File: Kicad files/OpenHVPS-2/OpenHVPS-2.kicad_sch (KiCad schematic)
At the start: 69 parts, among them J1 Conn_01x03_Male, J2 Conn_01x03_Male, Q1 FQT7N10, Q2 BC846A, Q3 MMDT3906, U1 MAX6008AEUR+T, U2 74HC14, U3 MAX4162, U4 CD14538BM

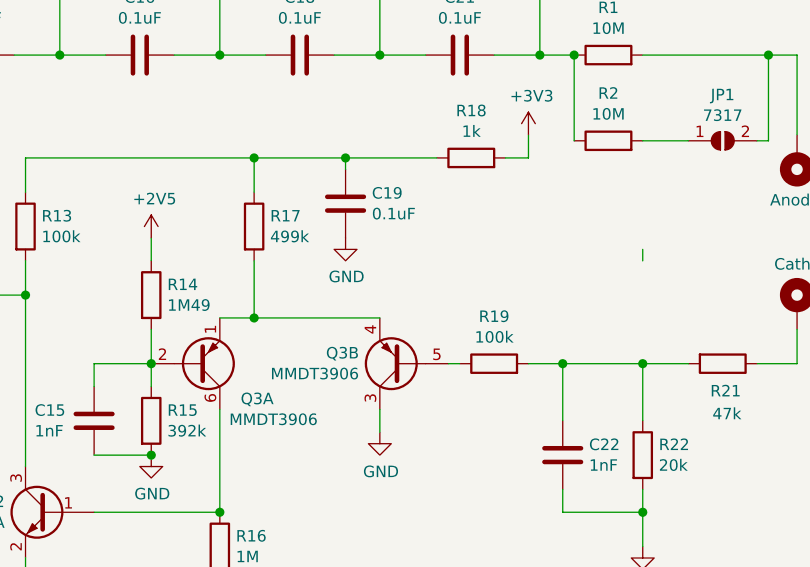
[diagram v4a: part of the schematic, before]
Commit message: Created BOM. updated component markings
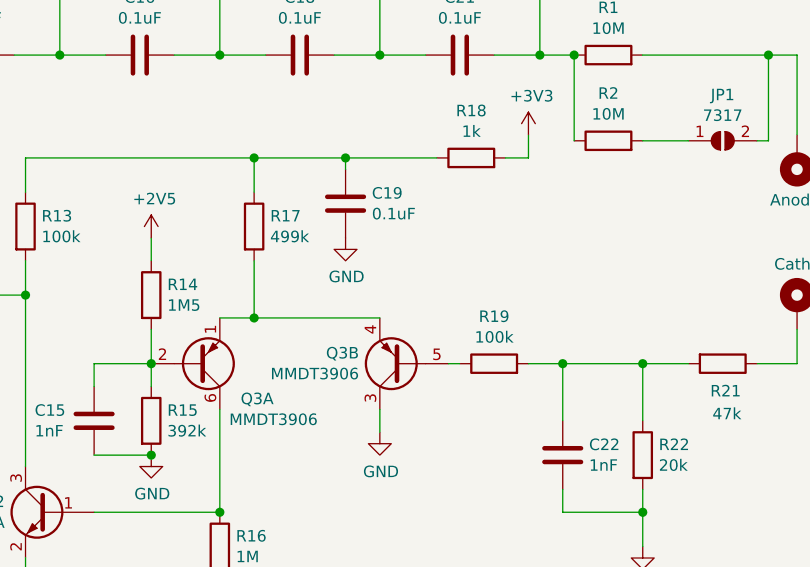
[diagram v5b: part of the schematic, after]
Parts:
- R14: value 1M49 -> 1M5
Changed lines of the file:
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@@
   (title_block
     (title "SafePulse")
-    (date "2021-01-15")
-    (rev "2.0")
+    (date "2021-01-17")
+    (rev "2.01")
     (company "SafeCast")
     (comment 1 "Double Sided Version")
@@
     (stroke (width 0) (type solid) (color 0 0 0 0))
   )
-  (wire (pts (xy 261.62 122.555) (xy 261.62 121.285))
-    (stroke (width 0) (type solid) (color 0 0 0 0))
-  )
   (wire (pts (xy 261.62 133.985) (xy 261.62 140.335))
     (stroke (width 0) (type solid) (color 0 0 0 0))
@@
       (effects (font (size 1.27 1.27)) hide)
     )
-    (property "Datasheet" "~" (id 3) (at 30.48 178.435 0)
+    (property "Datasheet" "https://www.digikey.com/en/products/detail/yageo/RC0805FR-073M16L/727809" (id 3) (at 30.48 178.435 0)
       (effects (font (size 1.27 1.27)) hide)
     )
@@
       (effects (font (size 1.27 1.27)) hide)
     )
-    (property "Datasheet" "~" (id 3) (at 40.64 125.095 0)
+    (property "Datasheet" "https://www.digikey.com/en/products/detail/yageo/RT0805FRE07560KL/1079317" (id 3) (at 40.64 125.095 0)
       (effects (font (size 1.27 1.27)) hide)
     )
@@
       (effects (font (size 1.27 1.27)) hide)
     )
-    (property "Datasheet" "~" (id 3) (at 53.34 99.695 0)
+    (property "Datasheet" "https://www.digikey.com/en/products/detail/stackpole-electronics-inc/RMCF0805FT100K/1760712" (id 3) (at 53.34 99.695 0)
       (effects (font (size 1.27 1.27)) hide)
     )
@@
       (effects (font (size 1.27 1.27)) hide)
     )
-    (property "Datasheet" "~" (id 3) (at 60.96 74.295 0)
+    (property "Datasheet" "https://www.digikey.com/en/products/detail/stackpole-electronics-inc/RMCF0805FT100K/1760712" (id 3) (at 60.96 74.295 0)
       (effects (font (size 1.27 1.27)) hide)
     )
@@
       (effects (font (size 1.27 1.27)) hide)
     )
-    (property "Datasheet" "~" (id 3) (at 71.12 37.465 0)
+    (property "Datasheet" "https://www.digikey.com/en/products/detail/te-connectivity-passive-product/CRG0805F100R/2380830" (id 3) (at 71.12 37.465 0)
       (effects (font (size 1.27 1.27)) hide)
     )
@@
       (effects (font (size 1.27 1.27)) hide)
     )
-    (property "Datasheet" "~" (id 3) (at 101.6 146.685 0)
+    (property "Datasheet" "https://www.digikey.com/en/products/detail/koa-speer-electronics-inc/RK73H2ATTD1213F/10235721" (id 3) (at 101.6 146.685 0)
       (effects (font (size 1.27 1.27)) hide)
     )
@@
       (effects (font (size 1.27 1.27)) hide)
     )
-    (property "Datasheet" "~" (id 3) (at 116.84 121.285 0)
+    (property "Datasheet" "https://www.digikey.com/en/products/detail/stackpole-electronics-inc/RMCF0805FT22M0/6053747" (id 3) (at 116.84 121.285 0)
       (effects (font (size 1.27 1.27)) hide)
     )
@@
       (effects (font (size 1.27 1.27)) hide)
     )
-    (property "Datasheet" "~" (id 3) (at 127 121.285 0)
+    (property "Datasheet" "https://www.digikey.com/en/products/detail/stackpole-electronics-inc/RMCF0805FT22M0/6053747" (id 3) (at 127 121.285 0)
       (effects (font (size 1.27 1.27)) hide)
     )
@@
       (effects (font (size 1.27 1.27)) hide)
     )
-    (property "Datasheet" "~" (id 3) (at 137.16 121.285 0)
+    (property "Datasheet" "https://www.digikey.com/en/products/detail/stackpole-electronics-inc/RMCF0805FT22M0/6053747" (id 3) (at 137.16 121.285 0)
       (effects (font (size 1.27 1.27)) hide)
     )
@@
       (effects (font (size 1.27 1.27)) hide)
     )
-    (property "Datasheet" "~" (id 3) (at 143.51 109.855 0)
+    (property "Datasheet" "https://www.digikey.com/en/products/detail/stackpole-electronics-inc/RMCF0805FT22M0/6053747" (id 3) (at 143.51 109.855 0)
       (effects (font (size 1.27 1.27)) hide)
     )
@@
       (effects (font (size 1.27 1.27)) hide)
     )
-    (property "Datasheet" "~" (id 3) (at 161.29 126.365 0)
+    (property "Datasheet" "https://www.digikey.com/en/products/detail/te-connectivity-passive-product/CRGCQ0805F33K/8576369" (id 3) (at 161.29 126.365 0)
       (effects (font (size 1.27 1.27)) hide)
     )
@@
       (effects (font (size 1.27 1.27)) hide)
     )
-    (property "Datasheet" "~" (id 3) (at 177.8 137.795 0)
+    (property "Datasheet" "https://www.digikey.com/en/products/detail/te-connectivity-passive-product/CRG0805F100R/2380830" (id 3) (at 177.8 137.795 0)
       (effects (font (size 1.27 1.27)) hide)
     )
@@
       (effects (font (size 1.27 1.27)) hide)
     )
-    (property "Datasheet" "~" (id 3) (at 193.04 118.745 0)
+    (property "Datasheet" "https://www.digikey.com/en/products/detail/stackpole-electronics-inc/RMCF0805FT100K/1760712" (id 3) (at 193.04 118.745 0)
       (effects (font (size 1.27 1.27)) hide)
     )
@@
       (effects (font (size 1.27 1.27)) (justify left))
     )
-    (property "Value" "1M49" (id 1) (at 208.788 127.514 0)
+    (property "Value" "1M5" (id 1) (at 208.788 127.514 0)
       (effects (font (size 1.27 1.27)) (justify left))
     )
@@
       (effects (font (size 1.27 1.27)) hide)
     )
-    (property "Datasheet" "~" (id 3) (at 207.01 126.365 0)
+    (property "Datasheet" "https://www.digikey.com/en/products/detail/vishay-dale/CRCW08051M50FKEA/1176034" (id 3) (at 207.01 126.365 0)
       (effects (font (size 1.27 1.27)) hide)
     )
@@
       (effects (font (size 1.27 1.27)) hide)
     )
-    (property "Datasheet" "~" (id 3) (at 207.01 140.335 0)
+    (property "Datasheet" "https://www.digikey.com/en/products/detail/yageo/RC0805FR-07392KL/727905" (id 3) (at 207.01 140.335 0)
       (effects (font (size 1.27 1.27)) hide)
     )
@@
       (effects (font (size 1.27 1.27)) hide)
     )
-    (property "Datasheet" "~" (id 3) (at 214.63 154.305 0)
+    (property "Datasheet" "https://www.digikey.com/en/products/detail/yageo/RT0805FRE071ML/1079056" (id 3) (at 214.63 154.305 0)
       (effects (font (size 1.27 1.27)) hide)
     )
@@
       (effects (font (size 1.27 1.27)) hide)
     )
-    (property "Datasheet" "~" (id 3) (at 218.44 118.745 0)
+    (property "Datasheet" "https://www.digikey.com/en/products/detail/stackpole-electronics-inc/RMCF0805FT499K/1760301" (id 3) (at 218.44 118.745 0)
       (effects (font (size 1.27 1.27)) hide)
     )
@@
       (effects (font (size 1.27 1.27)) hide)
     )
-    (property "Datasheet" "~" (id 3) (at 242.57 111.125 0)
+    (property "Datasheet" "https://www.digikey.com/en/products/detail/yageo/RT0805FRE071KL/1079055" (id 3) (at 242.57 111.125 0)
       (effects (font (size 1.27 1.27)) hide)
     )
@@
       (effects (font (size 1.27 1.27)) hide)
     )
-    (property "Datasheet" "~" (id 3) (at 245.11 133.985 0)
+    (property "Datasheet" "https://www.digikey.com/en/products/detail/stackpole-electronics-inc/RMCF0805FT100K/1760712" (id 3) (at 245.11 133.985 0)
       (effects (font (size 1.27 1.27)) hide)
     )
@@
       (effects (font (size 1.27 1.27)) hide)
     )
-    (property "Datasheet" "~" (id 3) (at 261.62 144.145 0)
+    (property "Datasheet" "https://www.digikey.com/en/products/detail/panasonic-electronic-components/ERJ-6ENF2002V/111532" (id 3) (at 261.62 144.145 0)
       (effects (font (size 1.27 1.27)) hide)
     )
@@
       (effects (font (size 1.27 1.27)) hide)
     )
-    (property "Datasheet" "~" (id 3) (at 270.51 133.985 0)
+    (property "Datasheet" "https://www.digikey.com/en/products/detail/yageo/RC0805FR-0747KL/727973" (id 3) (at 270.51 133.985 0)
       (effects (font (size 1.27 1.27)) hide)
     )
@@
     )
     (path "/adcc374e-3c86-48f4-8335-00f8a4e67511"
-      (reference "R14") (unit 1) (value "1M49") (footprint "Resistor_SMD:R_0805_2012Metric")
+      (reference "R14") (unit 1) (value "1M5") (footprint "Resistor_SMD:R_0805_2012Metric")
     )
     (path "/69a31fa7-1f19-4a47-87b1-54ebf66883f6"

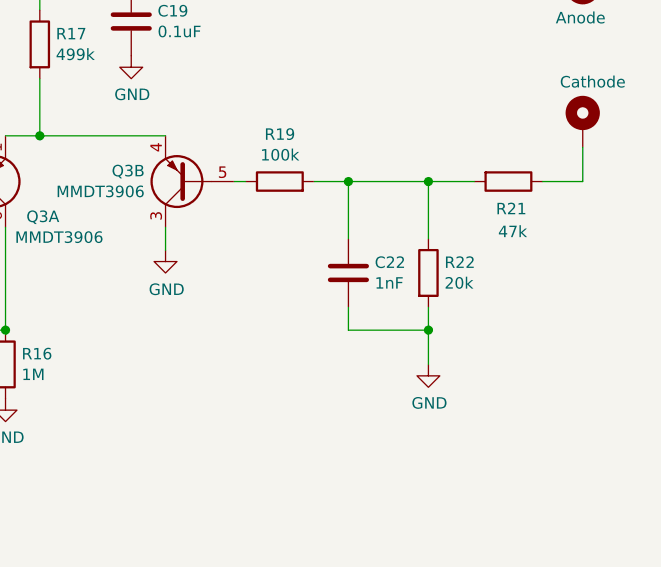
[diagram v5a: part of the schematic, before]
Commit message: updated C22 value
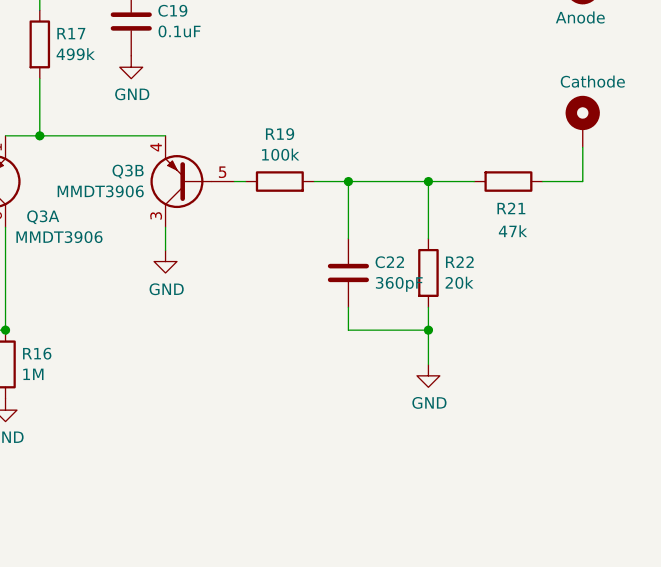
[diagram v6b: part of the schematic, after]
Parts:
- C22: value 1nF -> 360pF
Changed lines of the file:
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@@
       (effects (font (size 1.27 1.27)) (justify left))
     )
-    (property "Value" "1nF" (id 1) (at 255.651 145.294 0)
+    (property "Value" "360pF" (id 1) (at 255.651 145.294 0)
       (effects (font (size 1.27 1.27)) (justify left))
     )
@@
       (effects (font (size 1.27 1.27)) hide)
     )
-    (property "Datasheet" "https://www.digikey.com/en/products/detail/tdk-corporation/C1005X7R1H102K050BA/513719" (id 3) (at 252.73 144.145 0)
+    (property "Datasheet" "https://www.digikey.com/en/products/detail/kemet/C0805C361J1GAC7800/2212653" (id 3) (at 252.73 144.145 0)
       (effects (font (size 1.27 1.27)) hide)
     )
@@
     )
     (path "/743b7e51-503f-44bc-a063-83e91538f340"
-      (reference "C22") (unit 1) (value "1nF") (footprint "Capacitor_SMD:C_0805_2012Metric")
+      (reference "C22") (unit 1) (value "360pF") (footprint "Capacitor_SMD:C_0805_2012Metric")
     )
     (path "/00000000-0000-0000-0000-0000600ddc6a"

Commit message: deleting local files to allow pull
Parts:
- C1: value 0.1uF -> 150pF
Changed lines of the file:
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@@
       (effects (font (size 1.27 1.27)) (justify left))
     )
-    (property "Value" "0.1uF" (id 1) (at 48.641 93.218 0)
+    (property "Value" "150pF" (id 1) (at 48.641 93.218 0)
       (effects (font (size 1.27 1.27)) (justify left))
     )
@@
       (effects (font (size 1.27 1.27)) hide)
     )
-    (property "Datasheet" "https://www.digikey.com/en/products/detail/tdk-corporation/C2012X7T2E104K125AA/2733184" (id 3) (at 45.72 92.075 0)
+    (property "Datasheet" "https://www.digikey.com/en/products/detail/w%C3%BCrth-elektronik/885012207111/9346002" (id 3) (at 45.72 92.075 0)
       (effects (font (size 1.27 1.27)) hide)
     )
@@
     )
     (path "/00000000-0000-0000-0000-0000600fa622"
-      (reference "C1") (unit 1) (value "0.1uF") (footprint "Capacitor_SMD:C_0805_2012Metric")
+      (reference "C1") (unit 1) (value "150pF") (footprint "Capacitor_SMD:C_0805_2012Metric")
     )
     (path "/00000000-0000-0000-0000-0000600aa140"
